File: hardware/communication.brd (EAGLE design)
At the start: 33.5 x 34.6 mm, 44 parts, among them J1 MICRO_USB_B_HIROSE_ZX62-B-5PA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, U1 ES920LR3, U2 NJM12888F, X1 FA-238

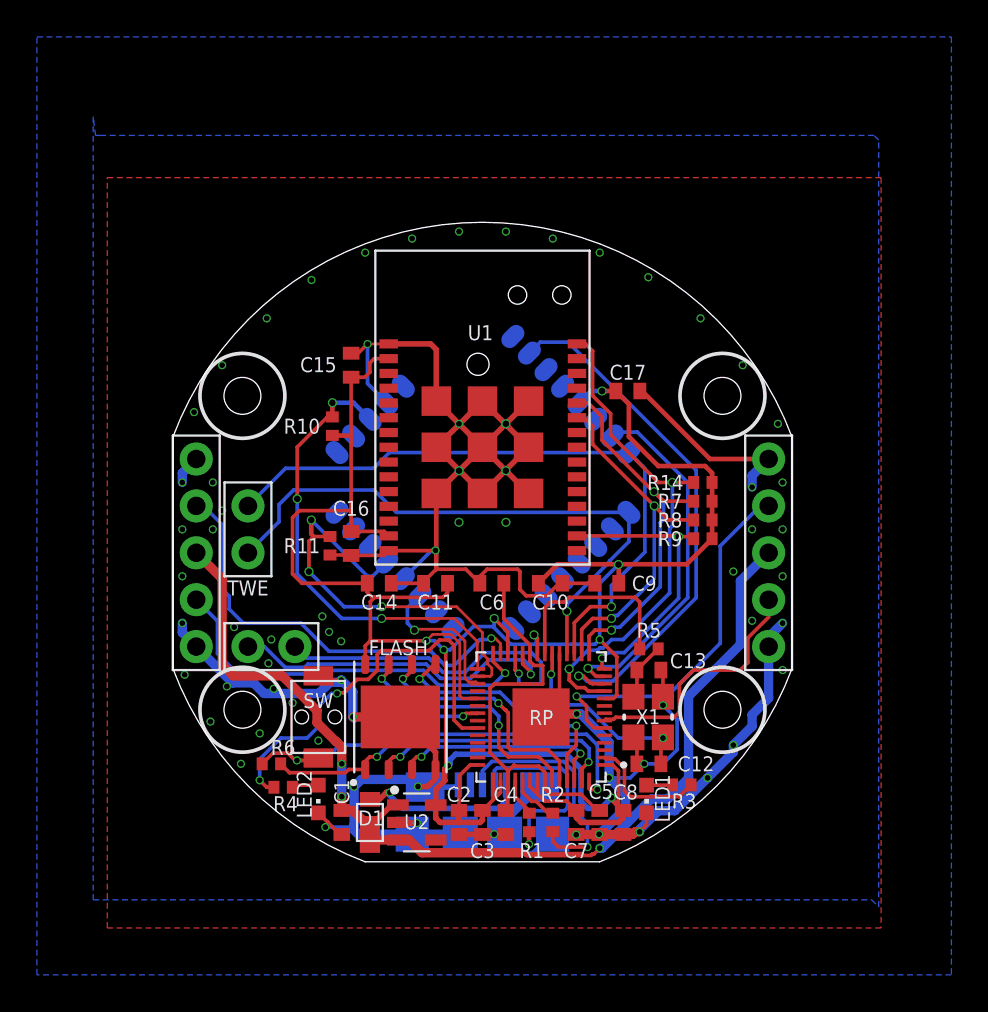
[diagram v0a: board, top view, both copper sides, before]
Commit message: LiPo回路修正，新LoRa
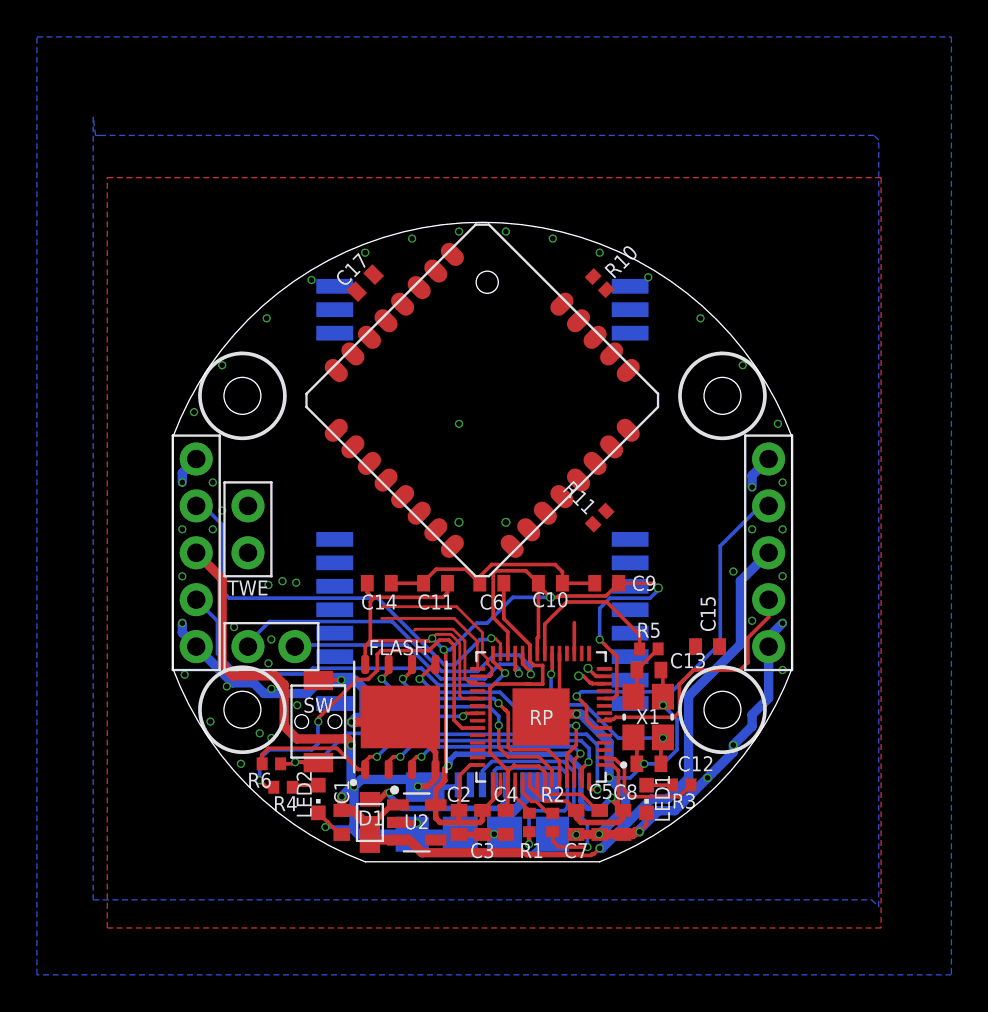
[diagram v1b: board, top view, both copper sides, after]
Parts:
- removed C16: 0.1µ, rcl:C0402
- removed R14, R7, R8, R9: 10k, rcl:R0402
- removed U1: ES920LR3, lora:ES920LR3
- added U$3: E220-900T22S, lora:E220-900T22S
- moved C15 24.6 mm to (12.2, -5.08), turned to 0 degrees
- moved U$1 20.3 mm to (-9.89, 8.25), flipped to the top
- moved R10 16.4 mm to (6.35, 14.6), turned to 135 degrees
- moved C17 15.4 mm to (-6.35, 14.6), turned to 45 degrees
- moved R11 14.7 mm to (6.35, 1.91), turned to 45 degrees
- moved SW 0.25 mm to (-8.89, -9.14)
- turned R6 to 180 degrees
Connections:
- removed net N$5: J1.ID
- removed net ROLA_!RESET!: R14.1, RP.11, U1.P30
- removed net ROLA_RTX: R8.1, RP.16, U1.P25
- removed net ROLA_TRX: R7.1, RP.15, U1.P26
- removed net WKUP: R9.1, RP.14, U1.P17
- new net LORA_AUX: RP.14, U$3.P9
- new net LORA_M0: RP.9, U$3.P5
- new net LORA_M1: RP.11, U$3.P6
- new net LORA_RTX: RP.16, U$3.P8
- new net LORA_TRX: RP.15, U$3.P7
- net GND: now also U$3.P1, U$3.P11, U$3.P13, U$3.P19, U$3.P2, U$3.P20, U$3.P22, U$3.P3, U$3.P4; no longer C16.1, U1.P1, U1.P15, U1.P31, U1.P32, U1.P33, U1.P34, U1.P35, U1.P36, U1.P37, U1.P38, U1.P39
- net VDD: now also U$3.P10; no longer C16.2, R14.2, R7.2, R8.2, R9.2, U1.P14, U1.P2
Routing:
- net GND: track 178.1 -> 118.5 mm, vias 68 -> 63
- net VDD: track 135.7 -> 97.8 mm, vias 9 -> 7
- net TWE_RTX: track 35.3 -> 2.24 mm, vias 1 -> 0
- net TWE_TRX: track 32.1 -> 0.00 mm, vias 1 -> 0
- net ROLA_!RESET!: track 27.5 -> 0.00 mm, vias 2 -> 0
- net TWE_PGM: track 29.0 -> 1.58 mm
- net ROLA_TRX: track 20.6 -> 0.00 mm, vias 2 -> 0
- net ROLA_RTX: track 19.5 -> 0.00 mm, vias 2 -> 0
- net TWE_RTS: track 19.6 -> 1.07 mm
- net TWE_SLEEP: track 25.4 -> 7.19 mm, vias 3 -> 0
- net WKUP: track 16.1 -> 0.00 mm, vias 2 -> 0
- net TWE_RESET: track 23.6 -> 9.34 mm, vias 3 -> 0
- net SWD: track 18.7 -> 14.8 mm
- net TWE_BPS: track 8.18 -> 5.85 mm, vias 1 -> 0
- net QSPI_SS: track 22.0 -> 23.9 mm
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
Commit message: ブランチテスト(ほとんど変更していません)
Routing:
- net VDD: track 97.8 -> 110.4 mm
- net TWE_SLEEP: track 7.19 -> 10.0 mm
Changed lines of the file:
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@@
 <wire x1="3.683" y1="-2.413" x2="1.651" y2="-2.413" width="0.2" layer="16"/>
 <wire x1="1.651" y1="-2.413" x2="0.254" y2="-3.81" width="0.2" layer="16"/>
-<wire x1="-5.220596875" y1="12.56735" x2="5.99644375" y2="14.958553125" width="0" layer="19" extent="1-1"/>
-<wire x1="-6.80961875" y1="14.145378125" x2="-5.220596875" y2="12.56735" width="0" layer="19" extent="1-1"/>
-<wire x1="-6.238" y1="-1.651" x2="-5.220596875" y2="12.56735" width="0" layer="19" extent="1-1"/>
+<wire x1="-5.22059375" y1="12.56735" x2="0.75635" y2="12.56735" width="0.1524" layer="1"/>
+<wire x1="0.75635" y1="12.56735" x2="3.683" y2="15.494" width="0.1524" layer="1"/>
+<wire x1="3.683" y1="15.494" x2="5.460996875" y2="15.494" width="0.1524" layer="1"/>
+<wire x1="5.460996875" y1="15.494" x2="5.99644375" y2="14.958553125" width="0.1524" layer="1"/>
+<wire x1="-5.22059375" y1="12.56735" x2="-6.80961875" y2="14.145378125" width="0" layer="19" extent="1-1"/>
+<wire x1="-6.238" y1="-1.651" x2="-5.22059375" y2="12.56735" width="0" layer="19" extent="1-1"/>
 <wire x1="8" y1="-6.895" x2="6.61" y2="-7.89" width="0" layer="19" extent="1-16"/>
 <wire x1="11.542" y1="-5.08" x2="9.525" y2="-1.905" width="0" layer="19" extent="1-1"/>
@@
 <wire x1="-0.2794" y1="-5.5767375" x2="-0.2794" y2="-4.8006" width="0.1524" layer="1"/>
 <wire x1="-5.461" y1="-3.556" x2="-1.524" y2="-3.556" width="0.1524" layer="1"/>
-<wire x1="6.10018125" y1="11.669325" x2="6.703553125" y2="14.25144375" width="0" layer="19" extent="1-1"/>
+<wire x1="6.703553125" y1="14.25144375" x2="6.703553125" y2="12.272696875" width="0.1524" layer="1"/>
+<wire x1="6.703553125" y1="12.272696875" x2="6.10018125" y2="11.669325" width="0.1524" layer="1"/>
 <wire x1="-0.26" y1="-6.29" x2="6.10018125" y2="11.669325" width="0" layer="19" extent="1-1"/>
 </signal>

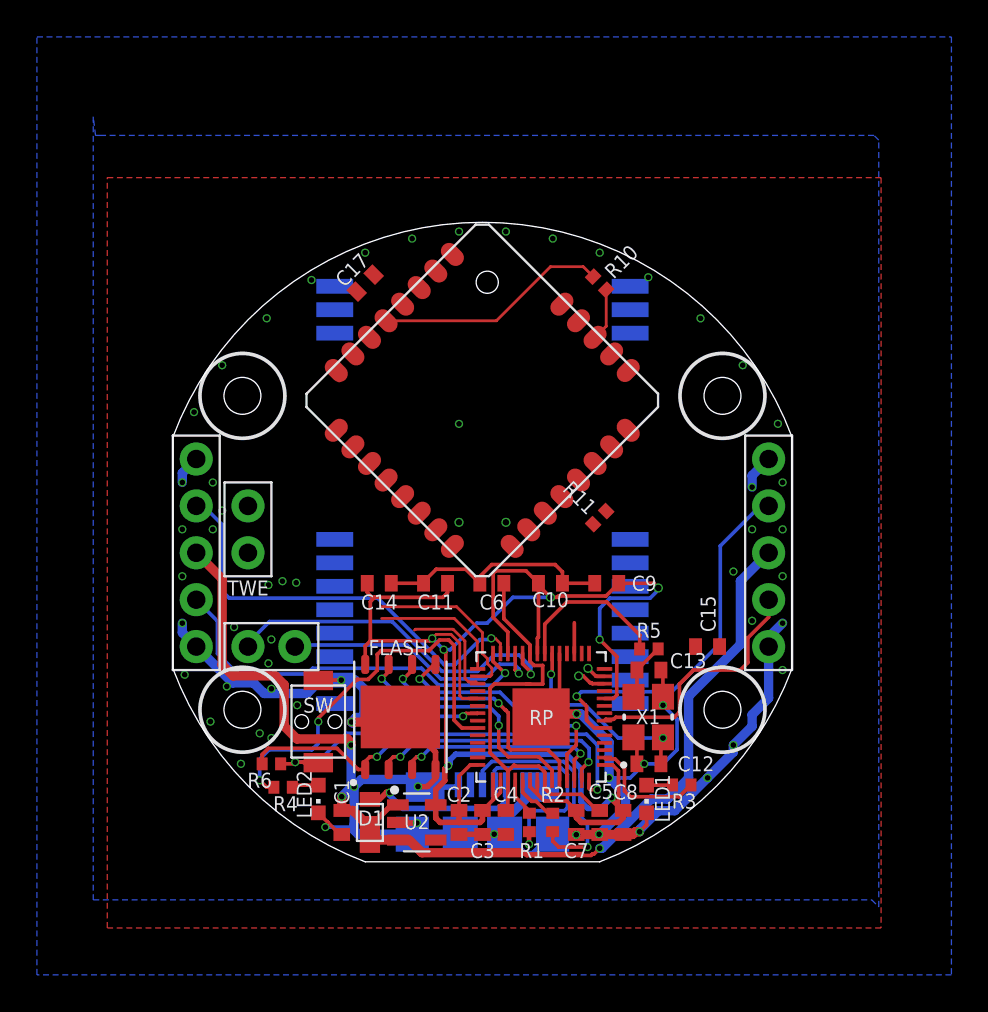
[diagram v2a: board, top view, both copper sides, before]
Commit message: issue#5:TELES/communication 基盤設計完了したので確認お願いします。
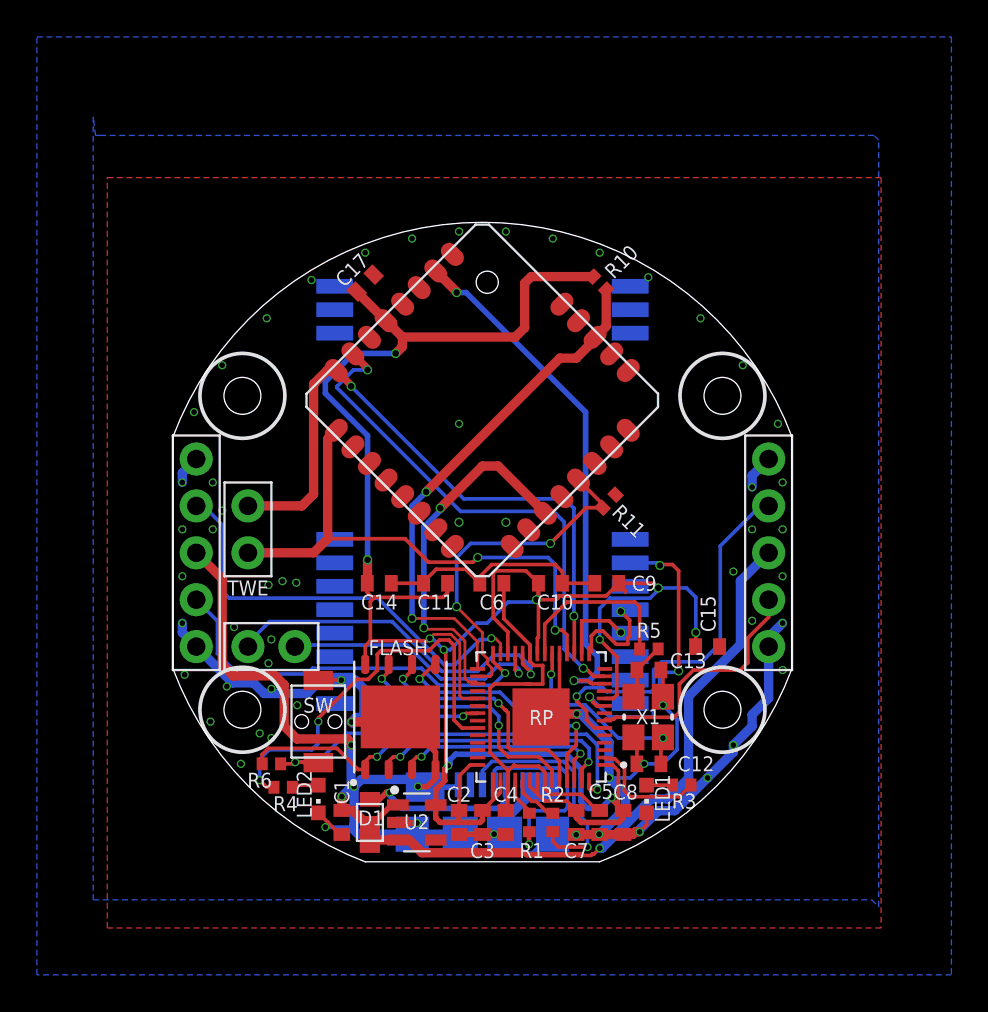
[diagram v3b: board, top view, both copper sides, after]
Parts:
- moved R11 1.02 mm to (6.86, 2.79), turned to 225 degrees
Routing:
- net TWE_RTX: track 2.24 -> 35.8 mm, vias 0 -> 2
- net TWE_TRX: track 0.00 -> 29.1 mm, vias 0 -> 2
- net TWE_PGM: track 1.58 -> 28.8 mm, vias 1 -> 2
- net TWE_RTS: track 1.07 -> 28.3 mm, vias 1 -> 2
- net VDD: track 110.4 -> 137.3 mm, vias 7 -> 10
- net TWE_SLEEP: track 10.0 -> 28.2 mm, vias 0 -> 2
- net LORA_M0: track 0.00 -> 16.9 mm, vias 0 -> 3
- net TWE_BPS: track 5.85 -> 19.9 mm, vias 0 -> 2
- net TWE_RESET: track 9.34 -> 19.0 mm, vias 0 -> 2
- net LORA_TRX: track 0.00 -> 5.39 mm, vias 0 -> 1
- net LORA_RTX: track 0.00 -> 4.15 mm, vias 0 -> 1
- net XOUT1: track 8.72 -> 9.62 mm
- net TX1: track 20.4 -> 21.2 mm

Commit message: communication_修正
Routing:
- net LORA_M1: track 0.00 -> 9.72 mm, vias 0 -> 1
- net VDD: track 137.3 -> 142.1 mm, vias 10 -> 11
- net LORA_AUX: track 0.00 -> 1.67 mm, vias 0 -> 1
- net LORA_TRX: track 5.39 -> 6.74 mm
- net TWE_RTX: track 35.8 -> 36.5 mm
- net TX1: track 21.2 -> 20.5 mm
- net XOUT1: track 9.62 -> 10.3 mm
- net TWE_PGM: track 28.8 -> 29.4 mm
- net LORA_RTX: track 4.15 -> 4.67 mm

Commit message: 回路微修正
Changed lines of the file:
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@@
 <param name="mdViaVia" value="5mil"/>
 <param name="mdSmdPad" value="5mil"/>
-<param name="mdSmdVia" value="5mil"/>
+<param name="mdSmdVia" value="0mil"/>
 <param name="mdSmdSmd" value="5mil"/>
 <param name="mdViaViaSameLayer" value="6mil"/>
@@
 <wire x1="9.271" y1="-1.651" x2="9.525" y2="-1.905" width="0.2" layer="1"/>
 <via x="9.525" y="-1.905" extent="1-16" drill="0.35"/>
-<wire x1="9.525" y1="-1.905" x2="8.807" y2="-1.187" width="0.2" layer="16"/>
-<wire x1="8.807" y1="-1.187" x2="6.56" y2="-1.187" width="0.2" layer="16"/>
+<wire x1="9.525" y1="-1.905" x2="9.525" y2="-1.397" width="0.2" layer="16"/>
+<wire x1="9.525" y1="-1.397" x2="9.315" y2="-1.187" width="0.2" layer="16"/>
+<wire x1="9.315" y1="-1.187" x2="6.56" y2="-1.187" width="0.2" layer="16"/>
 <wire x1="6.56" y1="-1.187" x2="5.969" y2="-1.778" width="0.2" layer="16"/>
 <wire x1="7.381" y1="-1.651" x2="6.692" y2="-2.34" width="0.2" layer="1"/>

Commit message: ベタ・シルク調整
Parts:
- moved C11 0.25 mm to (-2.54, -1.91)
- moved C14 0.25 mm to (-5.59, -1.91)
- moved C6 0.25 mm to (0.51, -1.91)
- moved C9 0.25 mm to (6.73, -1.91)
- moved C10 0.25 mm to (3.65, -1.90)
- renumbered U$3 to U1
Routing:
- net VDD: track 142.4 -> 144.5 mm
- net TWE_BPS: track 19.9 -> 18.0 mm
- net TWE_RESET: track 19.0 -> 20.2 mm
- net TWE_RTS: track 28.3 -> 27.1 mm
- net GND: track 118.1 -> 119.0 mm, vias 63 -> 146
- net XOUT1: track 10.3 -> 9.62 mm
